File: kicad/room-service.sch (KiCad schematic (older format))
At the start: 3 parts

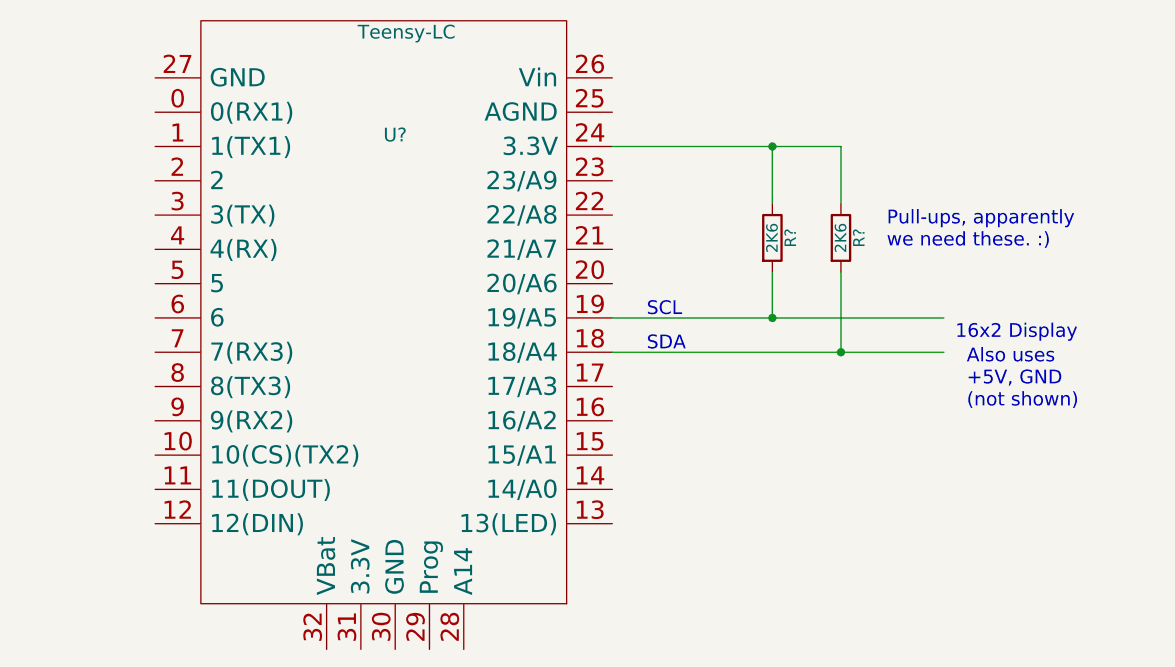
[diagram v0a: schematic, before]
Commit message: Add TLC5947 and keypad pins to schematic.
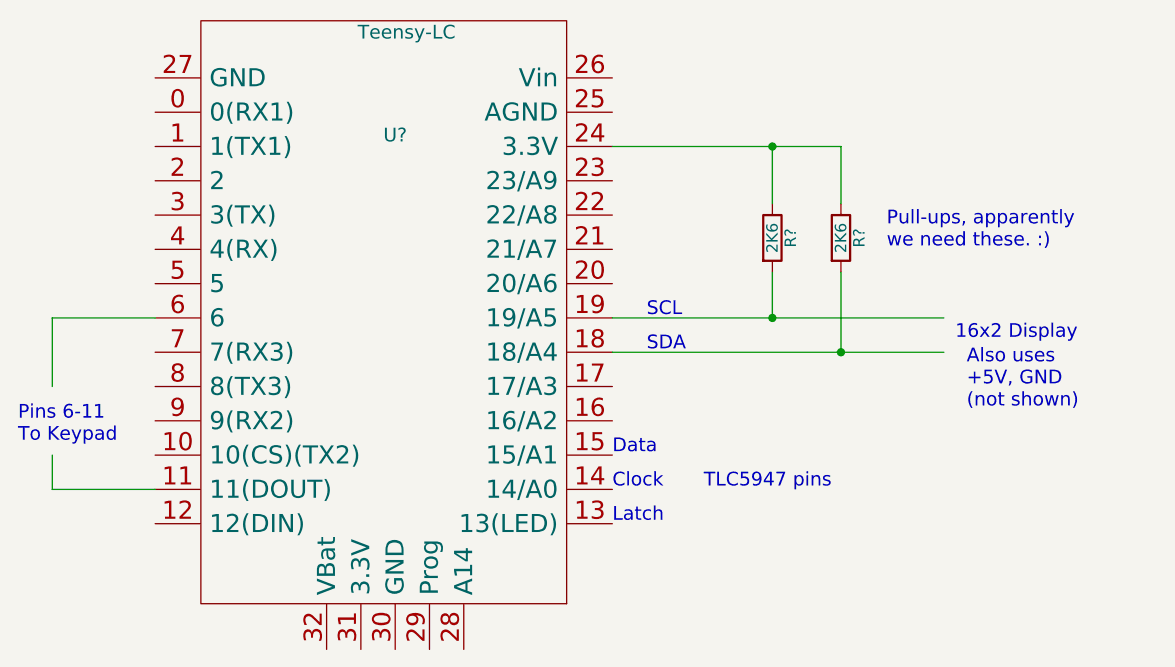
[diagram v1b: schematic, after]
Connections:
- wire segments 7 -> 11
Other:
- note added: "Clock"
- note added: "Data"
- note added: "Latch"
- note added: "Pins 6-11\nTo Keypad\n"
- note added: "TLC5947 pins"
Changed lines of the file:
@@
 Text Notes 8250 3900 0    60   ~ 0
 Also uses\n+5V, GND\n(not shown)\n
+Text Notes 6700 4400 0    60   ~ 0
+Latch
+Text Notes 6700 4250 0    60   ~ 0
+Clock
+Text Notes 6700 4100 0    60   ~ 0
+Data
+Text Notes 7100 4250 0    60   ~ 0
+TLC5947 pins
+Text Notes 4100 4050 0    60   ~ 0
+Pins 6-11\nTo Keypad\n
+Wire Wire Line
+	4700 3500 4250 3500
+Wire Wire Line
+	4250 3500 4250 3800
+Wire Wire Line
+	4700 4250 4250 4250
+Wire Wire Line
+	4250 4250 4250 4100
 $EndSCHEMATC

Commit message: kicad: Updated pin-outs
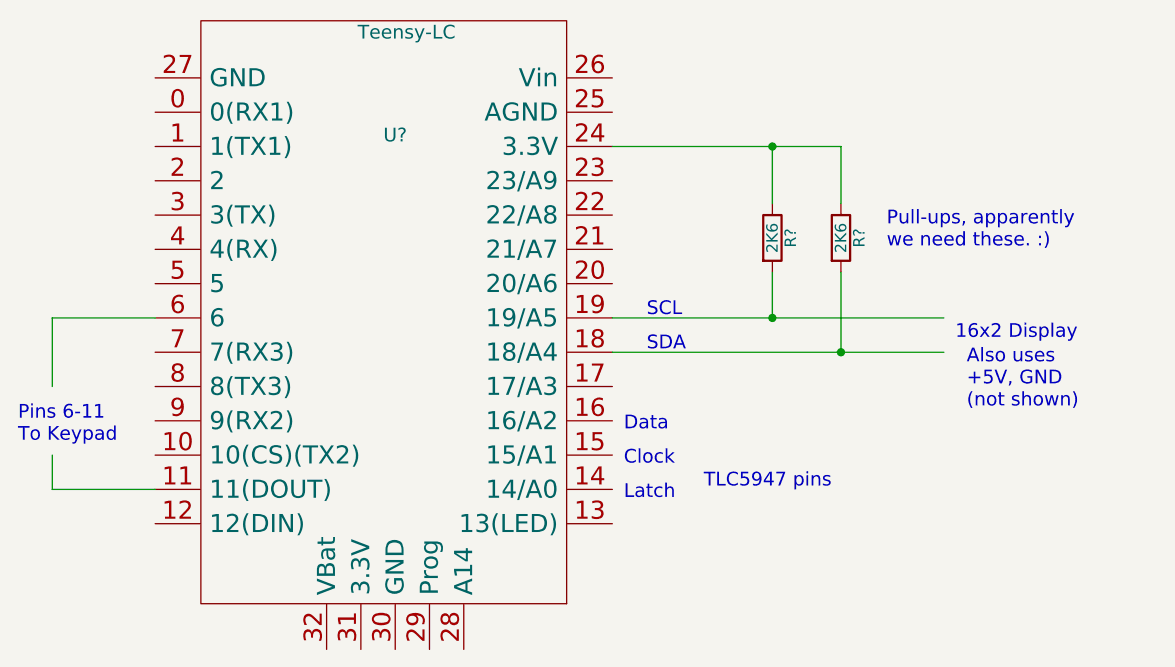
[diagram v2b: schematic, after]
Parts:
- renumbered 2K6 to R?
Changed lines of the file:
@@
 LIBS:teensy_3.1
 LIBS:freetronics_schematic
+LIBS:room-service-cache
 EELAYER 25 0
 EELAYER END
@@
 SCL\n
 $Comp
-L R 2K6
+L R R?
 U 1 1 57CD75BC
 P 7400 3150
@@
 Text Notes 8250 3900 0    60   ~ 0
 Also uses\n+5V, GND\n(not shown)\n
-Text Notes 6700 4400 0    60   ~ 0
+Text Notes 6750 4300 0    60   ~ 0
 Latch
-Text Notes 6700 4250 0    60   ~ 0
+Text Notes 6750 4150 0    60   ~ 0
 Clock
-Text Notes 6700 4100 0    60   ~ 0
+Text Notes 6750 4000 0    60   ~ 0
 Data
 Text Notes 7100 4250 0    60   ~ 0
